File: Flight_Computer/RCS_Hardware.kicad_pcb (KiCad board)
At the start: 2 copper layers, 50.8 x 50 mm, 57 parts, among them J1 SWD, J2 TYPE-C-31-M-12, J3 JST BATT, J4 3V3, J5 GND, J6 Solenoids, J7 Ext Sesnor, J8 Conn_01x05_Male, U1 STM32F401CCU6, U2 AMS1117-3.3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

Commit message: started new routing
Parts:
- removed C19: 100nF, Capacitor_SMD:C_0402_1005Metric
- removed R5, R6: 10k, Resistor_SMD:R_0402_1005Metric
- removed U3: BMP280, BMP280:XDCR_BMP280
- added C24: 0.1uF, Capacitor_SMD:C_0402_1005Metric, F.Cu at (110.3, 80.3)
- added C25: 10nF, Capacitor_SMD:C_0402_1005Metric, F.Cu at (113.3, 80.3)
- C21: value 22uF -> 0.1uF; footprint Capacitor_SMD:C_0805_2012Metric -> Capacitor_SMD:C_0402_1005Metric
- C22: value 22uF -> 2.2nF; footprint Capacitor_SMD:C_0805_2012Metric -> Capacitor_SMD:C_0402_1005Metric
- C4: footprint Capacitor_SMD:C_0603_1608Metric -> Capacitor_SMD:C_0402_1005Metric
- J3: value JST BATT -> SPI; footprint Connector_JST:JST_EH_B2B-EH-A_1x02_P2.50mm_Vertical -> Connector_PinHeader_2.54mm:PinHeader_1x08_P2.54mm_Vertical
- J4: value 3V3 -> 5V
- J7: value Ext Sesnor -> SPI; footprint Connector_PinHeader_2.54mm:PinHeader_1x04_P2.54mm_Vertical -> Connector_PinHeader_2.54mm:PinHeader_1x08_P2.54mm_Vertical
- U6: value AMS1117-3.3 -> MPU-6050; footprint Package_TO_SOT_SMD:SOT-223-3_TabPin2 -> Sensor_Motion:InvenSense_QFN-24_4x4mm_P0.5mm
- U7: value LT1690N8 -> LTC1690N8
- moved H1 73.2 mm to (104.1, 71.8)
- moved J3 60.9 mm to (102.6, 79.5)
- moved J6 58.4 mm to (110.2, 71.1), turned to 90 degrees
- moved D1 48.7 mm to (113.8, 89.2)
- moved U6 46.8 mm to (111.5, 77.0), turned to 0 degrees
- moved R3 46.4 mm to (113.0, 90.7), turned to 0 degrees
- moved C22 46.0 mm to (111.3, 73.7)
- moved H4 45.5 mm to (150.1, 106.7)
- moved J8 44.3 mm to (150.1, 77.7)
- moved C21 43.1 mm to (113.3, 73.7), turned to 0 degrees
- moved C13 42.3 mm to (110.3, 89.4), turned to 0 degrees
- moved J2 36.8 mm to (132.8, 74.6), turned to 0 degrees
- moved U2 36.0 mm to (113.1, 84.6), turned to 0 degrees
- moved C14 35.5 mm to (110.3, 91.4)
- moved C20 32.6 mm to (122.4, 73.7), turned to 0 degrees
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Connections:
- C21 pad 1: /BATT_IN -> Net-(U6-REGOUT)
- C22 pad 1: +3.3V -> Net-(U6-CPOUT)
- C23 pad 1: +3.3V -> VBUS
- J3 pad 1: /BATT_IN -> /CS1
- J3 pad 2: GND -> /MOSI2
- J4 pad 1: +3.3V -> VBUS
- J7 pad 1: +3.3V -> /CS2
- J7 pad 2: /SDA -> /MOSI2
- J7 pad 3: /SCL -> /MISO2
- J7 pad 4: GND -> /SCK
- U6 pad 1: GND -> /CLKIN
- U6 pad 2: +3.3V -> unconnected-(U6-NC-Pad2)
- U6 pad 3: /BATT_IN -> unconnected-(U6-NC-Pad3)
- U7 pad 1: +3.3V -> VBUS
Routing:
- net +3.3V: track 234.1 -> 0.00 mm, vias 10 -> 0
- net GND: track 126.7 -> 0.00 mm, vias 43 -> 0
- net /SDA: track 59.7 -> 0.00 mm, vias 4 -> 0
- net /SCL: track 56.9 -> 0.00 mm, vias 3 -> 0
- net /LED_G: track 49.0 -> 0.00 mm, vias 2 -> 0
- net /LED_B: track 47.5 -> 0.00 mm, vias 2 -> 0
- net /S6: track 45.8 -> 0.00 mm, vias 1 -> 0
- net /S5: track 45.7 -> 0.00 mm, vias 1 -> 0
- net /S4: track 45.5 -> 0.00 mm, vias 1 -> 0
- net /S1: track 41.6 -> 0.00 mm, vias 3 -> 0
- net /S3: track 39.0 -> 0.00 mm, vias 1 -> 0
- net /S2: track 38.3 -> 0.00 mm, vias 1 -> 0
- net /TX: track 34.2 -> 0.00 mm, vias 1 -> 0
- net /NRST: track 33.7 -> 0.00 mm, vias 2 -> 0
- net /RX: track 32.7 -> 0.00 mm, vias 1 -> 0
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- removed copper zone on B.Cu, net GND
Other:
- board size 50.8 x 50 mm -> 9.2 x 5.7 mm
- board text removed: "+"
- board text removed: "-"
- board text removed: "GND"
- board text removed: "L1"
- board text removed: "L2"
- board text removed: "NRST"
- board text removed: "SARP RCS Flight Computer V1.0"
- board text removed: "SWCLK"
- board text removed: "SWDIO"

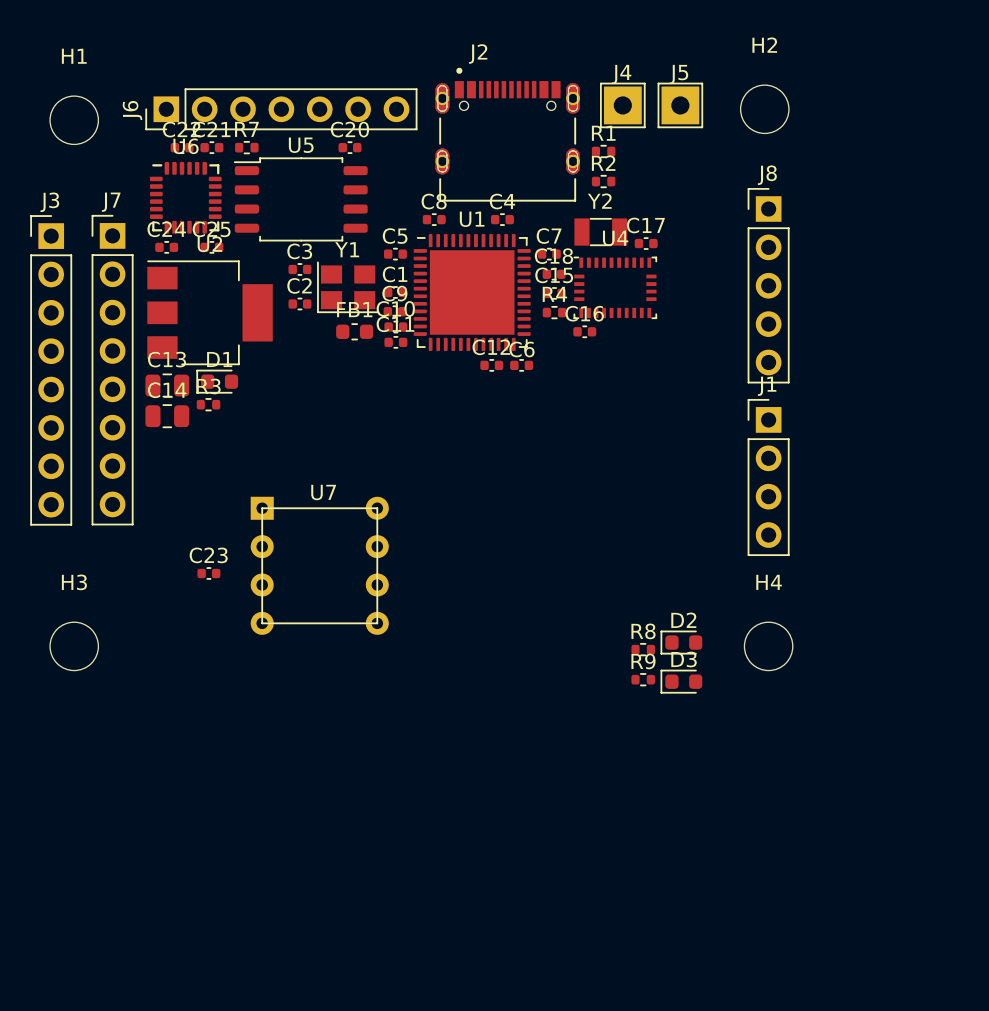
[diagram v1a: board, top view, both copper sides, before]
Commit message: condensed pcb components
haven't started actually routing yet--committing before that in case I mess it up.
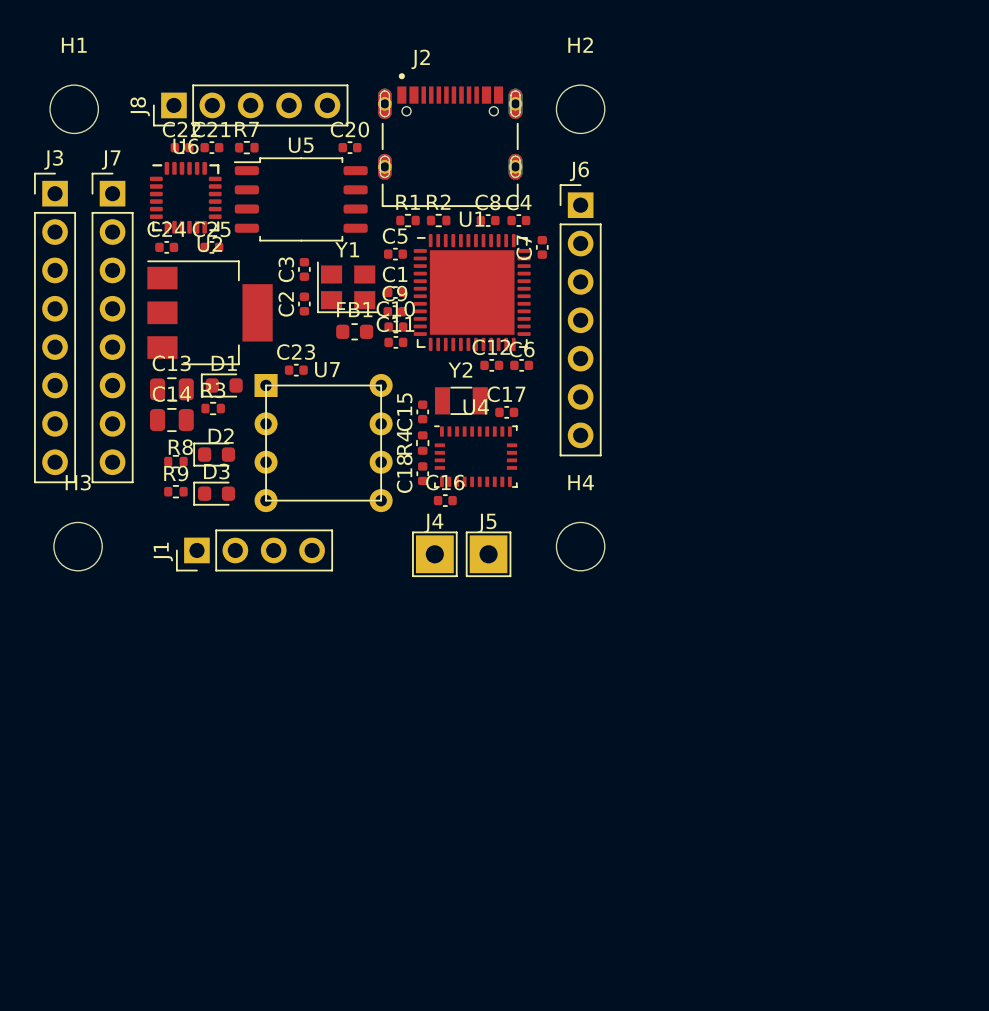
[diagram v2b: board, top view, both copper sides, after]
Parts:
- moved J8 40.0 mm to (110.7, 70.9), turned to 90 degrees
- moved J1 38.8 mm to (112.3, 100.3), turned to 90 degrees
- moved D3 33.3 mm to (113.6, 96.6)
- moved D2 33.3 mm to (113.6, 94.0)
- moved R8 33.3 mm to (110.9, 94.4)
- moved R9 33.3 mm to (110.9, 96.4)
- moved J5 32.3 mm to (131.6, 100.6)
- moved J4 32.2 mm to (128.0, 100.6)
- moved J6 28.2 mm to (137.7, 77.5), turned to 0 degrees
- moved C18 15.8 mm to (127.2, 95.2), turned to 90 degrees
- moved C23 14.7 mm to (118.8, 88.4)
- moved C16 14.5 mm to (128.7, 97.0)
- moved C17 14.5 mm to (132.8, 91.2)
- moved U4 14.5 mm to (130.7, 94.1)
- moved Y2 14.5 mm to (129.8, 90.4)
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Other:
- board size 9.2 x 5.7 mm -> 9.3 x 5.7 mm

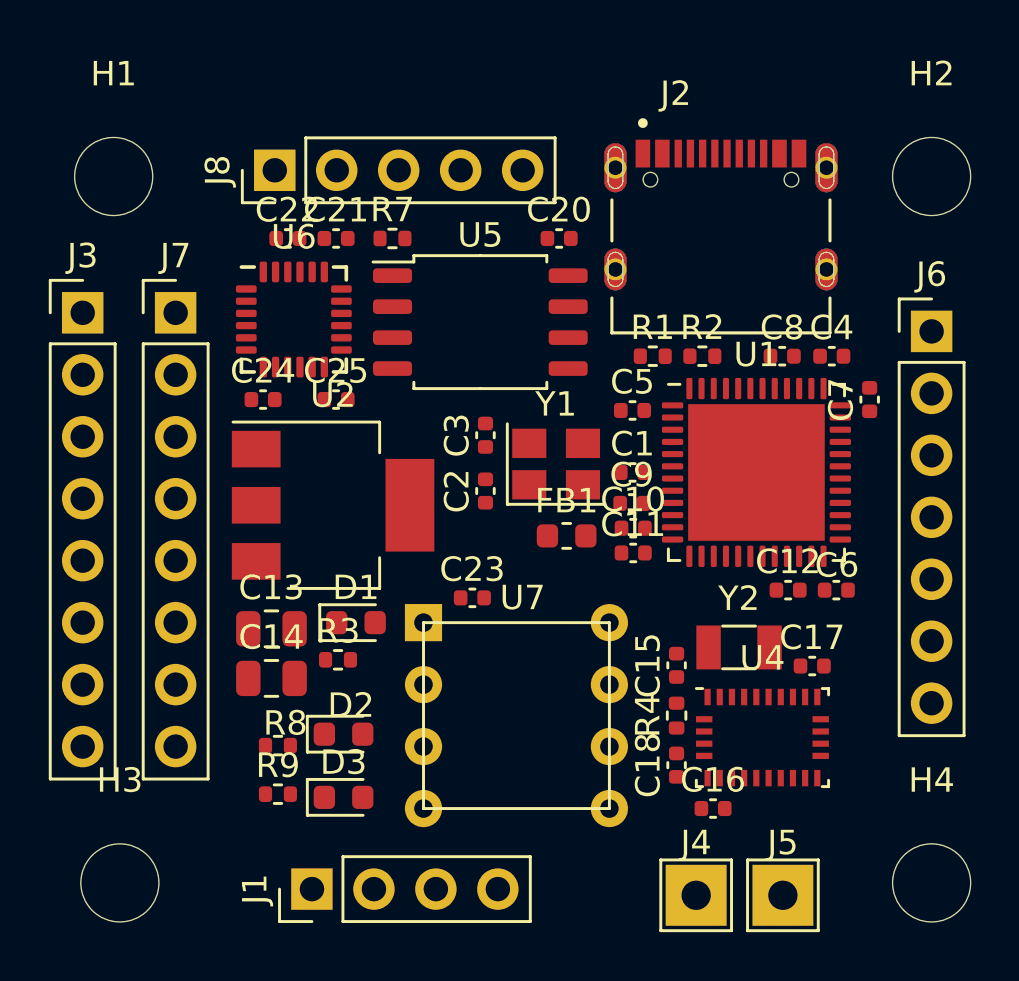
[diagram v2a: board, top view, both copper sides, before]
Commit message: routed LEDs & LTC (no GND)
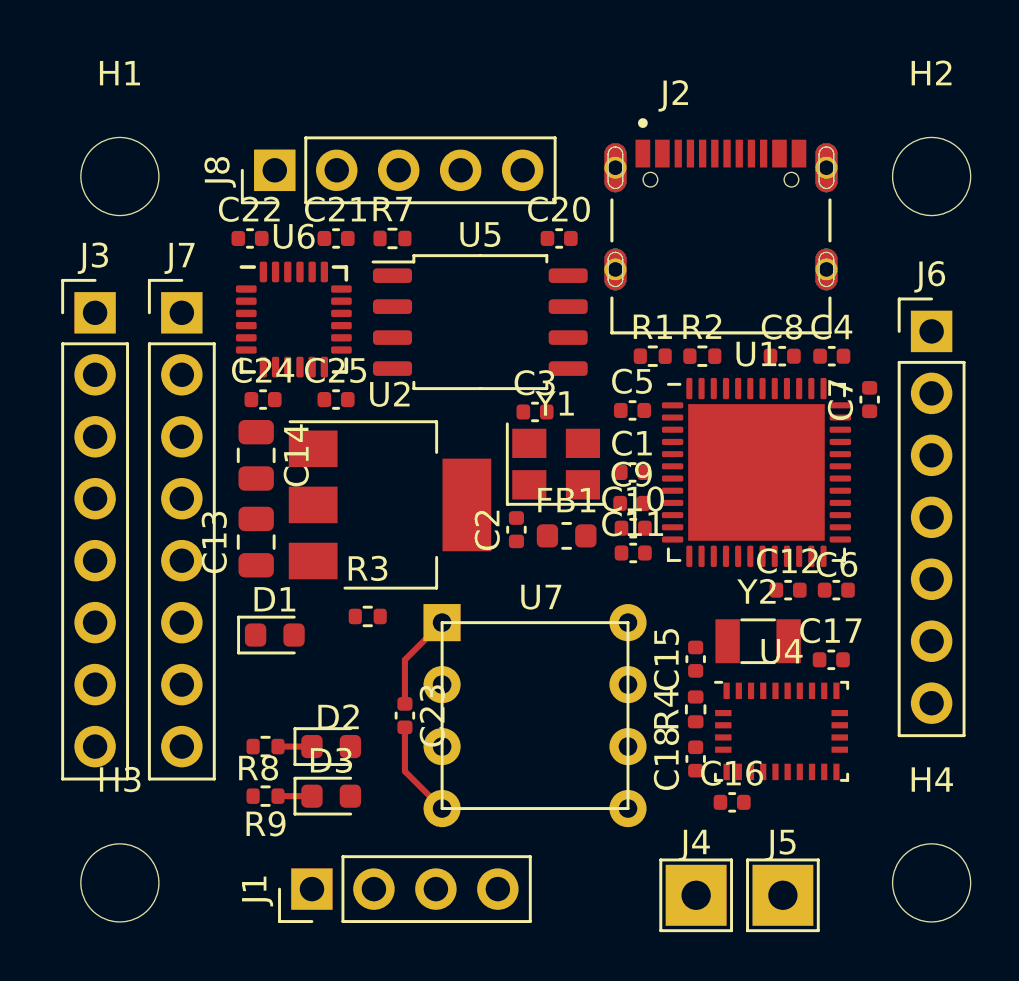
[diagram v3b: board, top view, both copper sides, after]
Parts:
- moved C14 9.17 mm to (110.0, 82.5), turned to -90 degrees
- moved C23 5.56 mm to (116.1, 93.2), turned to -90 degrees
- moved C13 3.61 mm to (110.0, 86.1), turned to 90 degrees
- moved D1 3.37 mm to (110.7, 89.9)
- moved U2 2.34 mm to (115.5, 84.6)
- moved C3 2.24 mm to (121.4, 80.8), turned to 0 degrees
- moved R3 2.15 mm to (114.6, 89.2)
- moved C2 2.03 mm to (120.7, 85.6)
- moved C22 1.55 mm to (109.7, 73.7)
- moved C17 0.82 mm to (133.6, 90.9)
- moved Y2 0.82 mm to (130.6, 90.2)
- moved C15 0.82 mm to (128.0, 90.9)
- moved C18 0.82 mm to (128.0, 95.0)
- moved R4 0.82 mm to (128.0, 93.0)
- moved C16 0.82 mm to (129.5, 96.8)
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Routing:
- net GND: track 0.00 -> 3.96 mm
- net VBUS: track 0.00 -> 3.96 mm
- net Net-(D3-K): track 0.00 -> 1.39 mm
- net Net-(D2-K): track 0.00 -> 1.39 mm

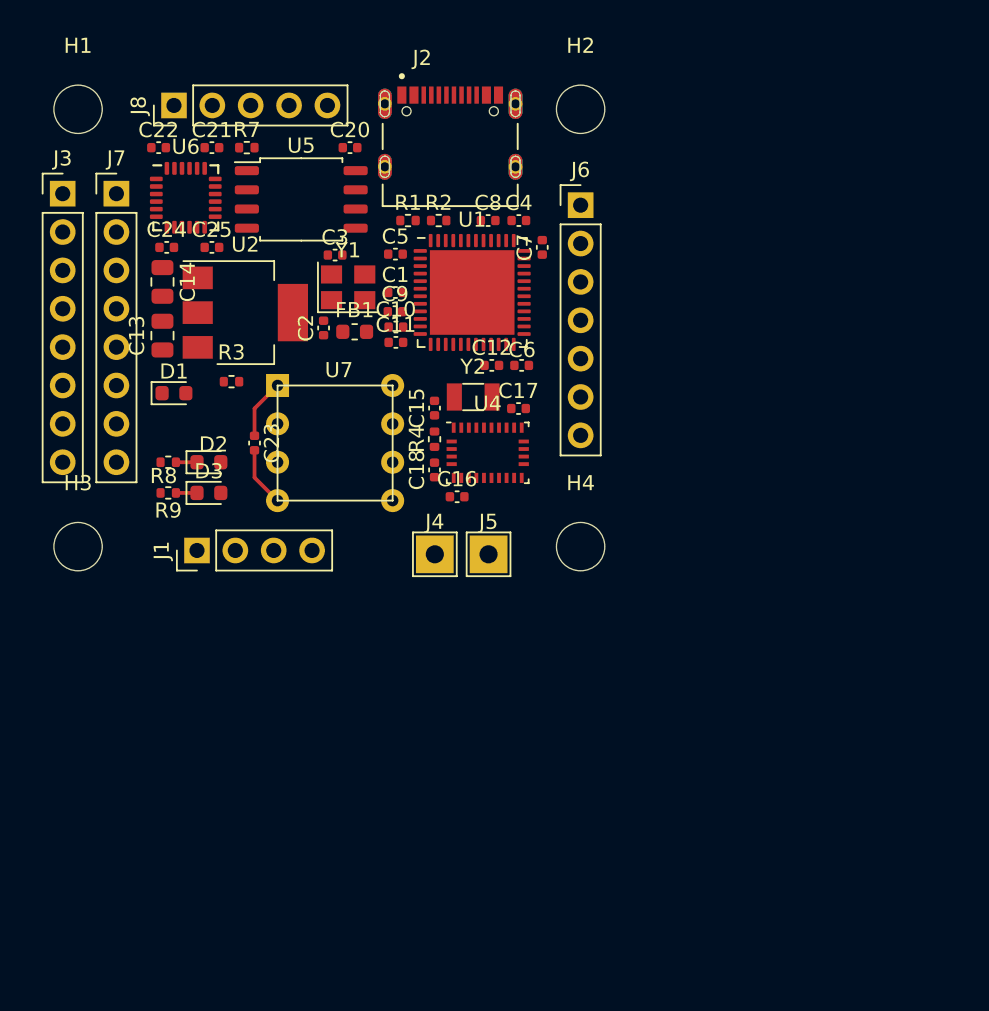
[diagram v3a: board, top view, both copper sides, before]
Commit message: expanded components & more routing
60x60mm edge cut, ground copper fill layers.
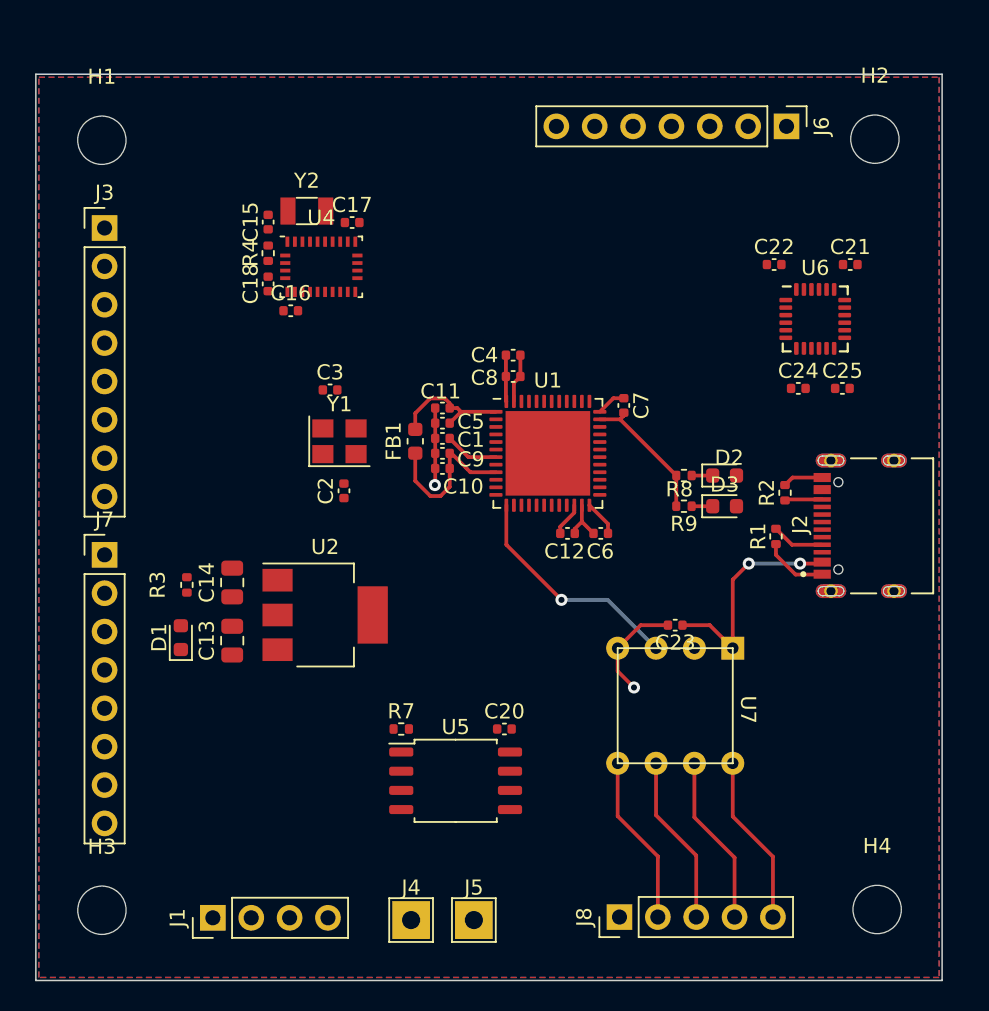
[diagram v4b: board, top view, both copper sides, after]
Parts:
- moved J8 61.3 mm to (140.2, 124.6)
- moved C21 43.0 mm to (155.5, 81.4)
- moved C24 42.8 mm to (152.1, 89.6)
- moved C25 42.8 mm to (155.0, 89.6)
- moved U6 42.4 mm to (153.2, 85.0)
- moved C22 41.5 mm to (150.5, 81.4)
- moved C20 39.8 mm to (132.6, 112.2)
- moved R7 39.8 mm to (125.8, 112.2)
- moved U5 39.8 mm to (129.4, 115.6)
- moved J2 37.8 mm to (158.4, 98.7), turned to 90 degrees
- moved U7 34.8 mm to (147.7, 106.8), turned to -90 degrees
- moved D2 34.2 mm to (147.2, 95.4)
- moved D3 34.2 mm to (147.2, 97.4)
- moved R8 34.2 mm to (144.5, 95.4)
- moved R9 34.2 mm to (144.5, 97.4)
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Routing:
- net GND: track 3.96 -> 34.8 mm, vias 0 -> 2
- net +3.3V: track 0.00 -> 15.8 mm
- net /TX: track 0.00 -> 15.4 mm, vias 0 -> 1
- net VBUS: track 3.96 -> 15.6 mm, vias 0 -> 2
- net Net-(J8-Pin_2): track 0.00 -> 11.3 mm
- net Net-(J8-Pin_4): track 0.00 -> 11.3 mm
- net Net-(J8-Pin_5): track 0.00 -> 11.3 mm
- net Net-(J8-Pin_3): track 0.00 -> 11.3 mm
- net +3.3VA: track 0.00 -> 10.6 mm
- net /NRST: track 0.00 -> 3.58 mm
- net Net-(J2-CC1): track 0.00 -> 3.50 mm
- net Net-(J2-CC2): track 0.00 -> 2.49 mm
- net Net-(U1-VCAP1): track 0.00 -> 2.25 mm
- added copper zone on B.Cu, net GND
- added copper zone on F.Cu, net GND
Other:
- board size 9.3 x 5.7 mm -> 60 x 60 mm
- board text added: "C10"

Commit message: uhhhh more routing
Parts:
- moved C3 7.41 mm to (126.5, 94.8), turned to 90 degrees
- moved FB1 6.48 mm to (129.5, 98.9), turned to 180 degrees
- moved C2 5.82 mm to (126.5, 92.6)
- moved C11 2.30 mm to (130.8, 90.7), turned to 90 degrees
- moved Y1 2.04 mm to (123.7, 93.7), turned to -90 degrees
- moved C10 1.98 mm to (130.3, 95.8), turned to 90 degrees
- moved C9 1.96 mm to (129.2, 95.8), turned to 90 degrees
- moved C1 1.84 mm to (129.8, 94.2)
- moved C5 1.78 mm to (129.8, 90.7), turned to 90 degrees
- moved C4 0.41 mm to (133.0, 87.8)
- moved C8 0.31 mm to (133.0, 89.0)
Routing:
- net /OSC_IN: track 0.00 -> 10.1 mm
- net /OSC_OUT: track 0.00 -> 8.49 mm
- net +3.3VA: track 10.6 -> 3.35 mm
- net +3.3V: track 15.8 -> 9.40 mm
- net /NRST: track 3.58 -> 1.82 mm
- net GND: track 34.8 -> 33.4 mm, vias 2 -> 1

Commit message: more routing!
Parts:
- moved J6 52.6 mm to (150.7, 124.8)
- moved J7 34.4 mm to (133.7, 80.0), turned to 90 degrees
- moved J8 19.6 mm to (158.8, 118.1), turned to 180 degrees
- moved R4 16.2 mm to (115.8, 96.8), turned to 0 degrees
- moved R7 14.0 mm to (139.3, 116.0)
- moved C15 12.4 mm to (113.2, 90.4), turned to -90 degrees
- moved U4 11.6 mm to (117.0, 92.7)
- moved C16 11.4 mm to (115.8, 95.6), turned to 180 degrees
- moved D2 11.1 mm to (141.0, 86.1)
- moved D3 11.1 mm to (141.0, 88.1)
- moved R8 11.1 mm to (138.3, 86.1)
- moved R9 11.1 mm to (138.3, 88.1)
- moved C17 11.1 mm to (118.3, 88.8)
- moved C21 10.5 mm to (151.0, 90.8)
- moved Y2 9.57 mm to (116.5, 86.9), turned to 180 degrees
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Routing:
- net /S6: track 0.00 -> 28.3 mm
- net /S5: track 0.00 -> 26.5 mm
- net /S1: track 0.00 -> 26.3 mm
- net /S4: track 0.00 -> 24.6 mm
- net VBUS: track 15.6 -> 36.9 mm, vias 2 -> 0
- net +3.3V: track 9.40 -> 26.7 mm
- net /TX: track 15.4 -> 0.00 mm, vias 1 -> 0
- net /USB_D-: track 0.00 -> 13.0 mm
- net /USB_D+: track 0.00 -> 13.0 mm
- net /MISO: track 0.00 -> 12.5 mm
- net /MOSI: track 0.00 -> 11.9 mm, vias 0 -> 2
- net Net-(J8-Pin_2): track 11.3 -> 0.00 mm
- net Net-(J8-Pin_4): track 11.3 -> 0.00 mm
- net Net-(J8-Pin_5): track 11.3 -> 0.00 mm
- net Net-(J8-Pin_3): track 11.3 -> 0.00 mm
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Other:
- board size 60 x 60 mm -> 60 x 53.1 mm
